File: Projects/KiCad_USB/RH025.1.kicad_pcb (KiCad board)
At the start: 2 copper layers, 65 x 30 mm, 34 parts, among them IC1 FE1.1S, J1 POWER_JACKCOMBO

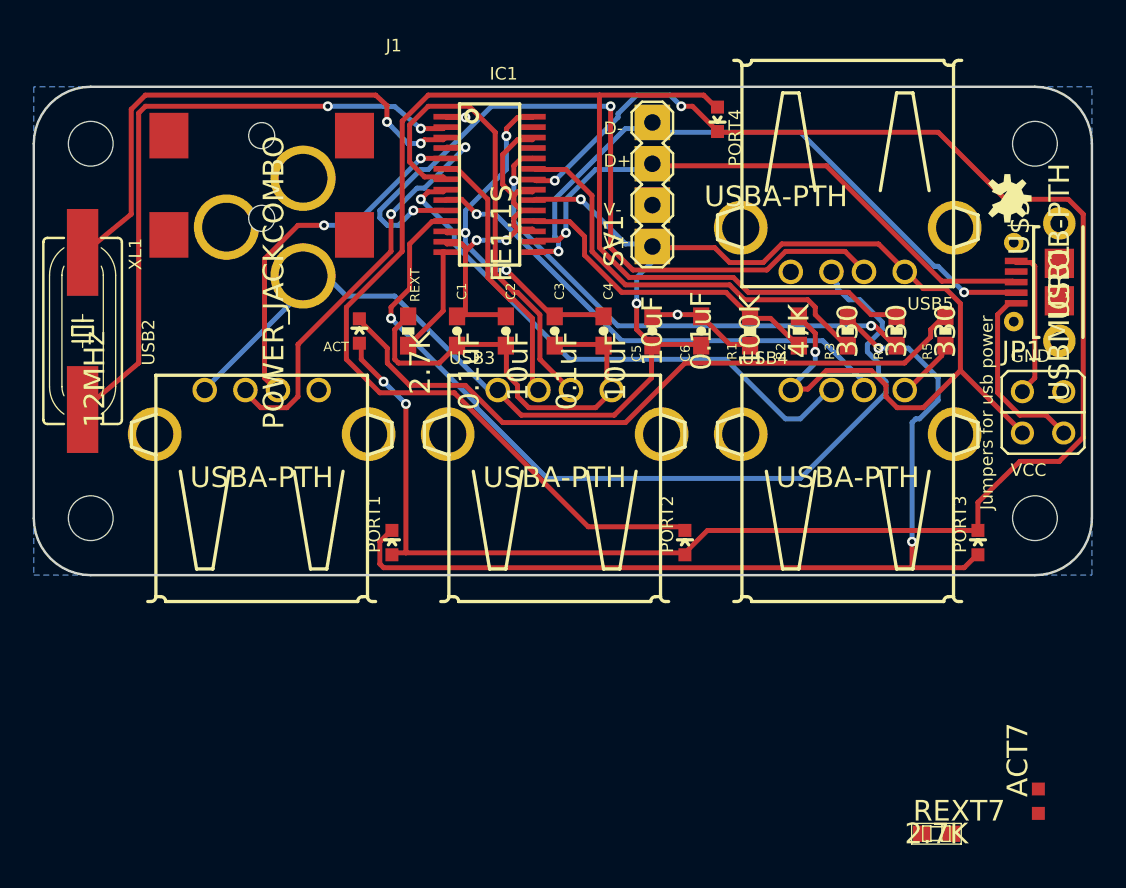
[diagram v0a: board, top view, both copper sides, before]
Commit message: Started work on cleaning up FE1.1s USB hub and VESC backplane
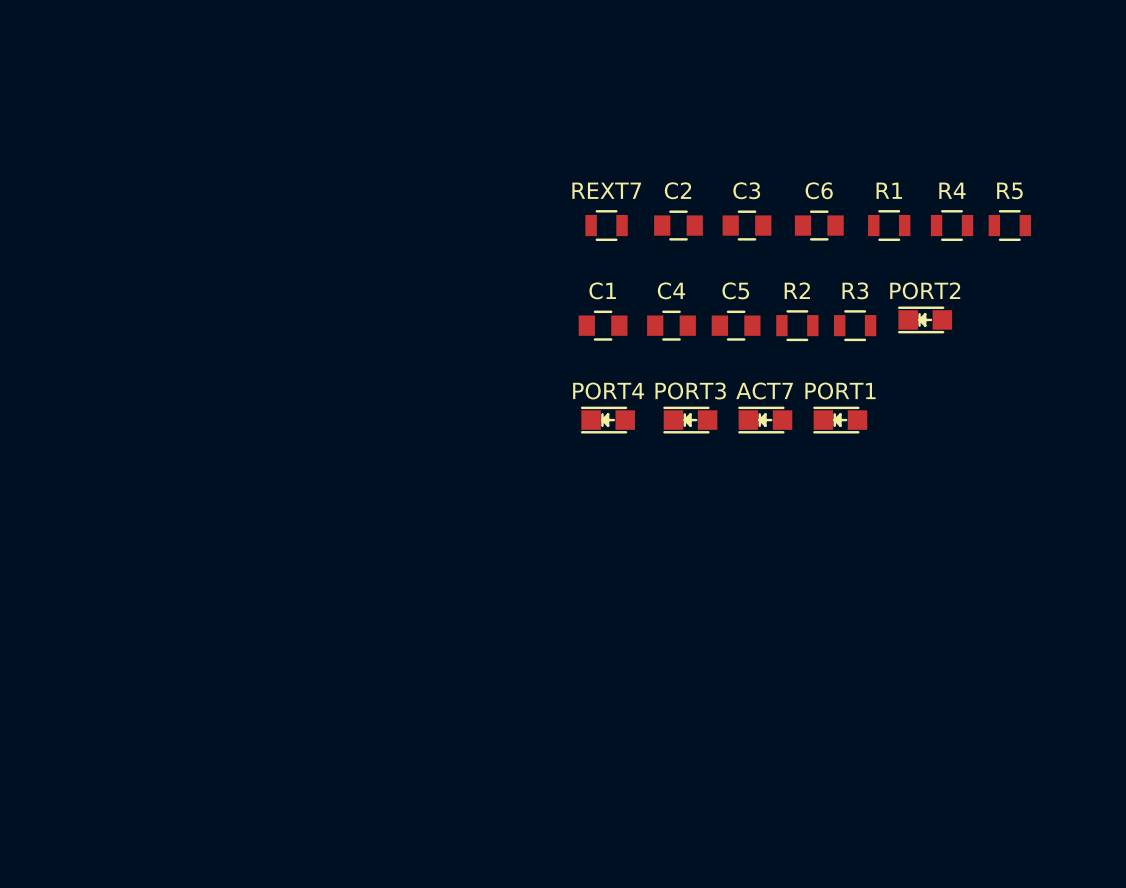
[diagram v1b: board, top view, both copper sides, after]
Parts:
- removed @HOLE0, @HOLE1, @HOLE2, @HOLE3: , 
- removed ACT: , LED-0603
- removed IC1: FE1.1S, FE1.1S_SSOP-28
- removed J1: POWER_JACKCOMBO, POWER_JACK_COMBO
- removed JP1: ~, JP2Q
- removed REXT: 2.7K, RES-0603
- removed SV1: ~, MA04-1
- removed U$3: , OSHW-LOGO-S
- removed USB1: USBMICROB-PTH, USB-MICROB-TH
- removed USB2, USB3, USB4, USB5: USBA-PTH, USB-A-F-PTH
- removed XL1: 12MHz, HC49UP
- ACT7, PORT1, PORT2, PORT3, PORT4: footprint LED-0603 -> LEDs:LED_0805
- C1, C2, C3, C4, C5, C6: footprint CAP-0603 -> Capacitors_SMD:C_0805
- R1, R2, R3, R4, R5, REXT7: footprint RES-0603 -> Resistors_SMD:R_0805
- moved REXT7 42.5 mm to (151.2, 98.5)
- moved ACT7 28.8 mm to (160.9, 110.5)
- moved PORT1 28.6 mm to (165.6, 110.5)
- moved PORT2 20.1 mm to (170.8, 104.3)
- moved PORT4 19.7 mm to (151.3, 110.5), turned to 0 degrees
- moved PORT3 19.2 mm to (156.3, 110.5)
- moved C3 13.5 mm to (159.8, 98.5), turned to 0 degrees
- moved C2 12.4 mm to (155.6, 98.5), turned to 0 degrees
- moved R1 10.7 mm to (168.6, 98.5), turned to 0 degrees
- moved C6 9.72 mm to (164.3, 98.5), turned to 0 degrees
- moved C1 8.98 mm to (151.0, 104.7), turned to 0 degrees
- moved R5 7.59 mm to (176.0, 98.5), turned to 0 degrees
- moved R4 7.32 mm to (172.4, 98.5), turned to 0 degrees
- moved C5 5.15 mm to (159.1, 104.7), turned to 0 degrees
- moved C4 4.19 mm to (155.2, 104.7), turned to 0 degrees
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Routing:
- net /N$25: track 113.5 -> 0.00 mm, vias 4 -> 0
- net VBUS: track 105.6 -> 0.00 mm, vias 3 -> 0
- net /N$6: track 90.9 -> 0.00 mm
- net /N$20: track 59.1 -> 0.00 mm, vias 2 -> 0
- net /N$11: track 54.6 -> 0.00 mm, vias 1 -> 0
- net /N$12: track 47.8 -> 0.00 mm, vias 2 -> 0
- net /N$22: track 42.2 -> 0.00 mm
- net /D-: track 39.5 -> 0.00 mm, vias 2 -> 0
- net /N$7: track 39.4 -> 0.00 mm, vias 2 -> 0
- net GND: track 38.4 -> 0.00 mm, vias 2 -> 0
- net /D+: track 35.8 -> 0.00 mm, vias 1 -> 0
- net /N$15: track 33.8 -> 0.00 mm, vias 1 -> 0
- net /N$9: track 31.9 -> 0.00 mm, vias 2 -> 0
- net /N$24: track 31.5 -> 0.00 mm, vias 2 -> 0
- net /N$14: track 30.9 -> 0.00 mm, vias 1 -> 0
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- removed copper zone on B.Cu, net GND
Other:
- board outline removed
- board text removed: "D+"
- board text removed: "D-"
- board text removed: "GND"
- board text removed: "Jumpers for usb power"
- board text removed: "REG"
- board text removed: "RH025.1 Dec 2015"
- board text removed: "V+"
- board text removed: "V-"
- board text removed: "VCC"
- board text removed: "piZero Hub Richard Hawthorn richardhawthorn.com"
